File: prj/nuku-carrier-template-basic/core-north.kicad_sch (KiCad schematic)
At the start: 3 parts, among them J3 DF40HC(4.0)-90DS-0.4V

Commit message: Route template.basic
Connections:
- net IO14_12_P renamed CLK
- net IO14_1_N renamed CONFIG_DIN_D01
- net IO14_1_P renamed CONFIG_MOSI_D00
- net IO14_2_N renamed CONFIG_D03
- net IO14_2_P renamed CONFIG_D02
- net IO14_6_P renamed CONFIG_FCS_B
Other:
- note added: "CLK -> IO_L12P_T1_MRCC_14 Multi-region clock"
- note removed: "CONFIG_D02"
- note removed: "CONFIG_D03"
- note removed: "CONFIG_DIN_D01"
- note removed: "CONFIG_FCS_B"
- note removed: "CONFIG_MOSI_D00"

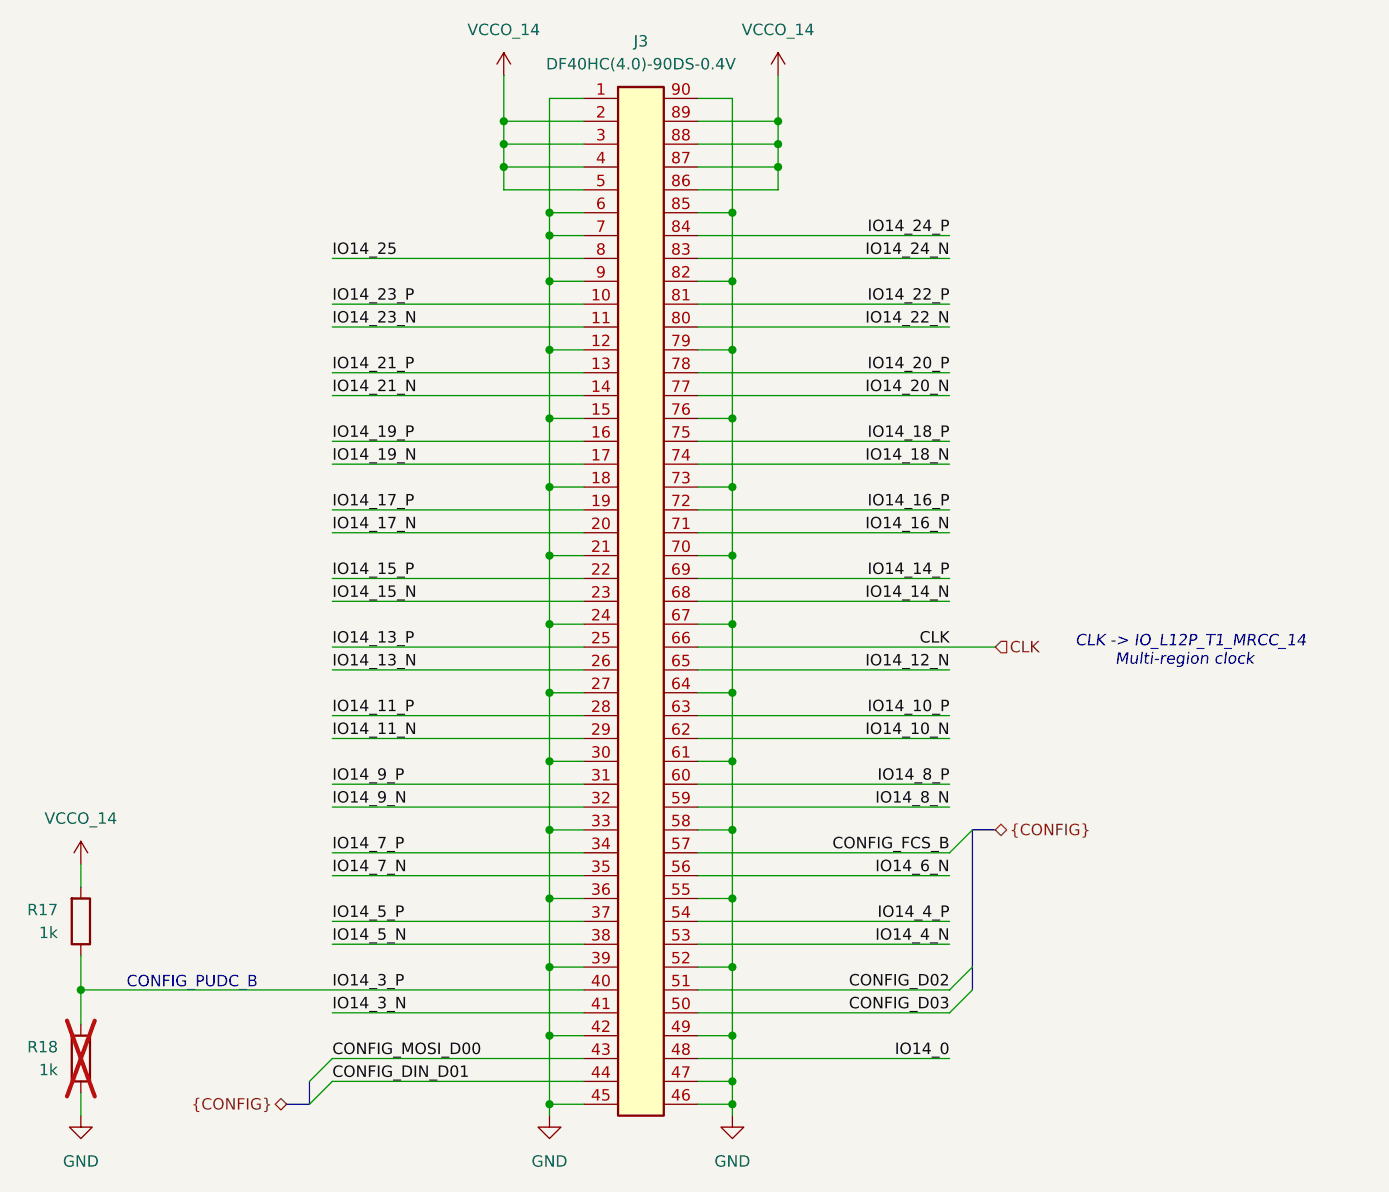
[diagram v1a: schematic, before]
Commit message: Finish template.basic + Production outputs
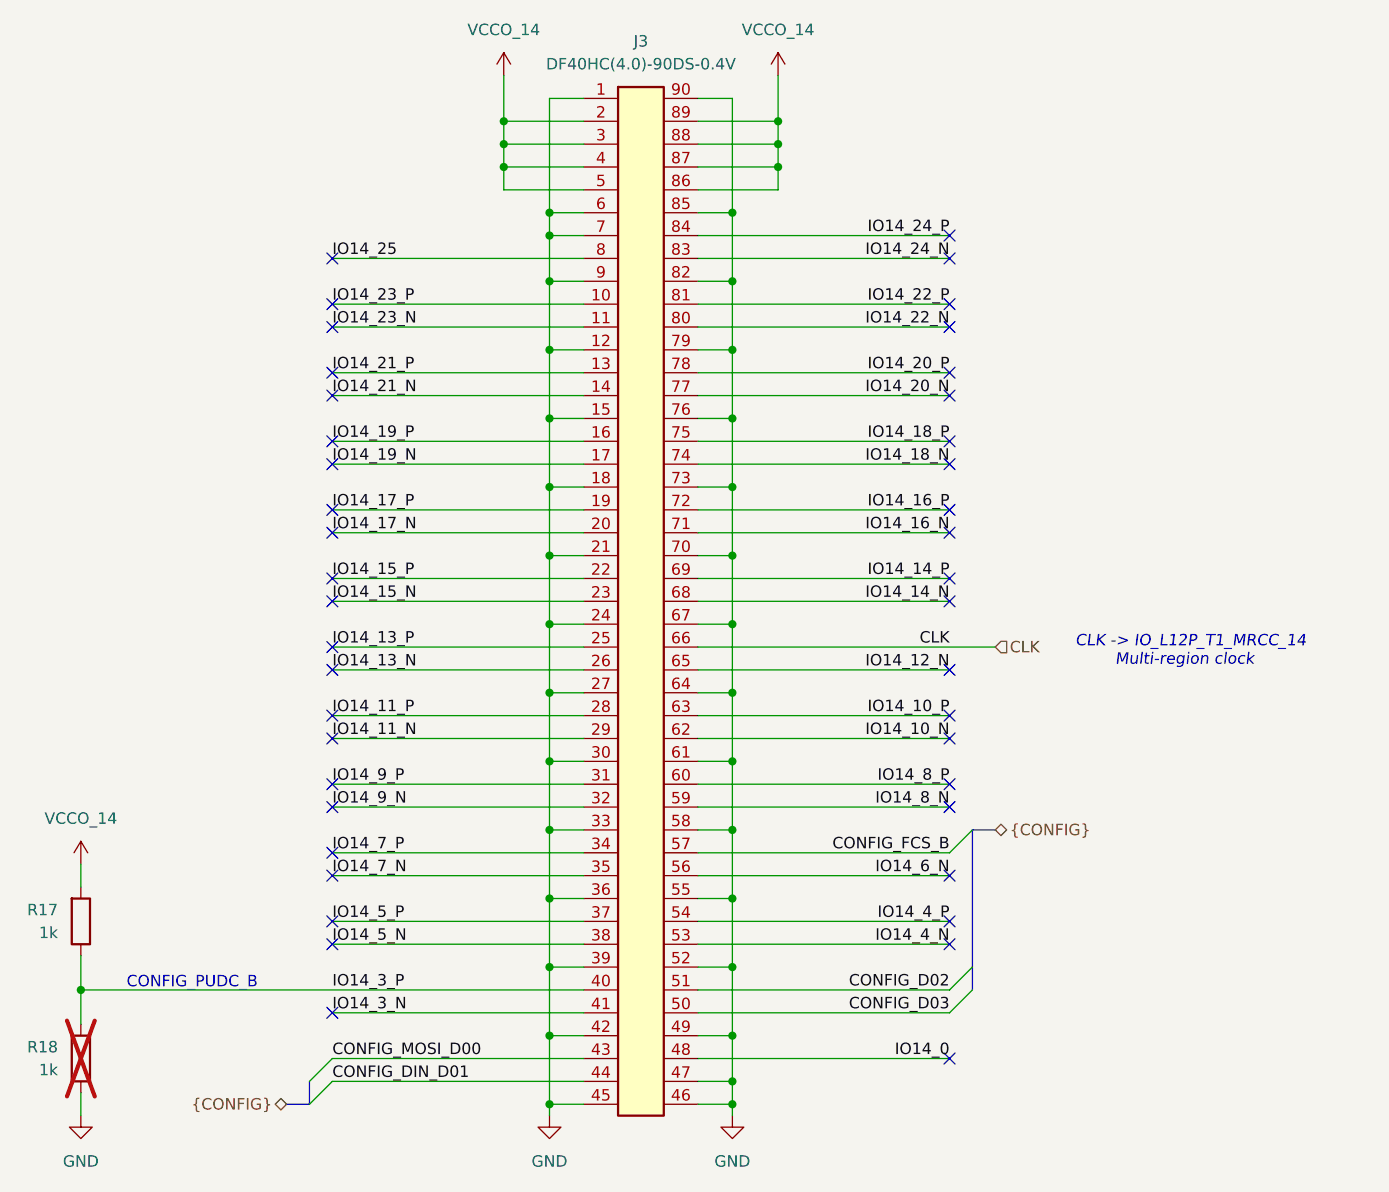
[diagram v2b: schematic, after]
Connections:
- no-connect marks 0 -> 43
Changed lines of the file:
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@@
 		(color 0 0 0 0)
+	)
+	(no_connect
+		(at 182.88 81.28)
+	)
+	(no_connect
+		(at 114.3 88.9)
+	)
+	(no_connect
+		(at 182.88 109.22)
+	)
+	(no_connect
+		(at 114.3 78.74)
+	)
+	(no_connect
+		(at 114.3 81.28)
+	)
+	(no_connect
+		(at 182.88 119.38)
+	)
+	(no_connect
+		(at 182.88 66.04)
+	)
+	(no_connect
+		(at 182.88 55.88)
+	)
+	(no_connect
+		(at 114.3 86.36)
+	)
+	(no_connect
+		(at 182.88 73.66)
+	)
+	(no_connect
+		(at 182.88 132.08)
+	)
+	(no_connect
+		(at 182.88 58.42)
+	)
+	(no_connect
+		(at 114.3 109.22)
+	)
+	(no_connect
+		(at 182.88 78.74)
+	)
+	(no_connect
+		(at 182.88 88.9)
+	)
+	(no_connect
+		(at 114.3 142.24)
+	)
+	(no_connect
+		(at 114.3 134.62)
+	)
+	(no_connect
+		(at 114.3 116.84)
+	)
+	(no_connect
+		(at 182.88 116.84)
+	)
+	(no_connect
+		(at 114.3 66.04)
+	)
+	(no_connect
+		(at 182.88 63.5)
+	)
+	(no_connect
+		(at 182.88 71.12)
+	)
+	(no_connect
+		(at 114.3 104.14)
+	)
+	(no_connect
+		(at 182.88 134.62)
+	)
+	(no_connect
+		(at 114.3 127)
+	)
+	(no_connect
+		(at 114.3 96.52)
+	)
+	(no_connect
+		(at 114.3 124.46)
+	)
+	(no_connect
+		(at 182.88 127)
+	)
+	(no_connect
+		(at 182.88 147.32)
+	)
+	(no_connect
+		(at 182.88 96.52)
+	)
+	(no_connect
+		(at 182.88 93.98)
+	)
+	(no_connect
+		(at 114.3 71.12)
+	)
+	(no_connect
+		(at 114.3 63.5)
+	)
+	(no_connect
+		(at 114.3 111.76)
+	)
+	(no_connect
+		(at 114.3 132.08)
+	)
+	(no_connect
+		(at 114.3 58.42)
+	)
+	(no_connect
+		(at 114.3 119.38)
+	)
+	(no_connect
+		(at 182.88 111.76)
+	)
+	(no_connect
+		(at 182.88 104.14)
+	)
+	(no_connect
+		(at 182.88 86.36)
+	)
+	(no_connect
+		(at 114.3 101.6)
+	)
+	(no_connect
+		(at 114.3 73.66)
+	)
+	(no_connect
+		(at 114.3 93.98)
 	)
 	(bus_entry

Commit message: Finish bridgeless template
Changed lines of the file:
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@@
 		(comment 1 "@supersmau")
+	)
+	(rectangle
+		(start 186.69 99.06)
+		(end 195.58 104.14)
+		(stroke
+			(width 0)
+			(type dash)
+		)
+		(fill
+			(type none)
+		)
+	)
+	(rectangle
+		(start 96.52 149.86)
+		(end 110.49 154.94)
+		(stroke
+			(width 0)
+			(type dash)
+		)
+		(fill
+			(type none)
+		)
+	)
+	(rectangle
+		(start 186.69 119.38)
+		(end 200.66 124.46)
+		(stroke
+			(width 0)
+			(type dash)
+		)
+		(fill
+			(type none)
+		)
 	)
 	(text "CONFIG_PUDC_B"

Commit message: Finish boards - prod ready
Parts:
- J3: footprint nuku:DF40HC(4.0)-90DS-0.4V -> nuku:DF40C-90DS-0.4V; symbol nuku:DF40HC(4.0)-90DS-0.4V -> nuku:DF40C-90DS-0.4V; LCSC C597947 -> C2911197
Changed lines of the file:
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@@
 			(justify left bottom)
-		)
-		(property "Netclass" "DIFF_92"
-			(at 135.89 139.7 0)
-			(effects
-				(font
-					(size 1.27 1.27)
-					(italic yes)
-				)
-				(justify right bottom)
-			)
 		)
 	)
@@
 	)
 	(symbol
-		(lib_name "DF40HC(4.0)-90DS-0.4V_1")
-		(lib_id "nuku:DF40HC(4.0)-90DS-0.4V")
+		(lib_id "nuku:DF40C-90DS-0.4V")
 		(at 146.05 39.37 0)
 		(unit 1)
@@
 			)
 		)
-		(property "Footprint" "nuku:DF40HC(4.0)-90DS-0.4V"
+		(property "Footprint" "nuku:DF40C-90DS-0.4V"
 			(at 146.05 156.21 0)
 			(effects
@@
 			)
 		)
-		(property "Datasheet" "https://www.lcsc.com/datasheet/lcsc_datasheet_2006112253_HRS-Hirose-DF40HC-4-0-90DS-0-4V-51_C597947.pdf"
+		(property "Datasheet" "https://www.lcsc.com/datasheet/lcsc_datasheet_2206011716_HRS-Hirose-DF40C-90DS-0-4V-51_C2911197.pdf"
 			(at 146.05 158.75 0)
 			(effects
@@
 			)
 		)
-		(property "LCSC" "C597947"
-			(at 146.05 39.37 0)
-			(effects
-				(font
-					(size 1.27 1.27)
-				)
-				(hide yes)
-			)
+		(property "LCSC" "C2911197"
+			(at 146.05 160.02 0)
+			(effects
+				(font
+					(size 1.27 1.27)
+				)
+				(justify left top)
+				(hide yes)
+			)
